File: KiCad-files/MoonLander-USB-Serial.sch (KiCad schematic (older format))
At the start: 7 parts, among them IC3 PRTR5V0U2X, IC4 CP2110-GM

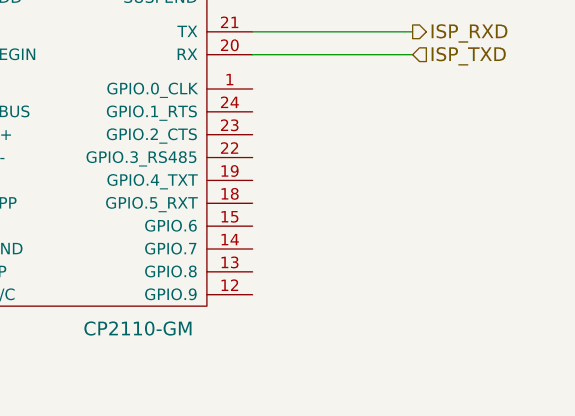
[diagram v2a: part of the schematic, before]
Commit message: drive ISP_ENTRY and RST from CP2110 GPIO outputs
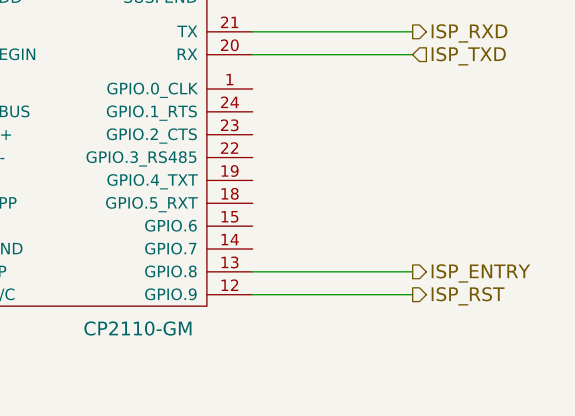
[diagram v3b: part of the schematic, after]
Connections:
- net ISP_RST: now reaches IC4.12 (GPIO.9)
- net ISP_ENTRY: now reaches IC4.13 (GPIO.8)
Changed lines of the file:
@@
 $EndComp
 $Comp
-L 5V_USB #PWR6
+L 5V_USB #PWR5
 U 1 1 565F94A8
 P 3100 3050
-F 0 "#PWR6" H 3100 2900 50  0001 C CNN
+F 0 "#PWR5" H 3100 2900 50  0001 C CNN
 F 1 "5V_USB" H 3100 3190 50  0000 C CNN
 F 2 "" H 3100 3050 60  0000 C CNN
@@
 $EndComp
 $Comp
-L GND #PWR7
+L GND #PWR6
 U 1 1 565F94C0
 P 3100 3400
-F 0 "#PWR7" H 3100 3150 50  0001 C CNN
+F 0 "#PWR6" H 3100 3150 50  0001 C CNN
 F 1 "GND" H 3100 3250 50  0000 C CNN
 F 2 "" H 3100 3400 50  0000 C CNN
@@
 	4650 4100 6200 4100
 $Comp
-L 5V_USB #PWR16
+L 5V_USB #PWR15
 U 1 1 565FB66D
 P 5000 3550
-F 0 "#PWR16" H 5000 3400 50  0001 C CNN
+F 0 "#PWR15" H 5000 3400 50  0001 C CNN
 F 1 "5V_USB" H 5000 3690 50  0000 C CNN
 F 2 "" H 5000 3550 60  0000 C CNN
@@
 	6050 3400 6200 3400
 $Comp
-L GND #PWR17
+L GND #PWR16
 U 1 1 565FBA98
 P 5000 4950
-F 0 "#PWR17" H 5000 4700 50  0001 C CNN
+F 0 "#PWR16" H 5000 4700 50  0001 C CNN
 F 1 "GND" H 5000 4800 50  0000 C CNN
 F 2 "" H 5000 4950 50  0000 C CNN
@@
 $EndComp
 $Comp
-L GND #PWR20
+L GND #PWR19
 U 1 1 565FBABC
 P 5400 3450
-F 0 "#PWR20" H 5400 3200 50  0001 C CNN
+F 0 "#PWR19" H 5400 3200 50  0001 C CNN
 F 1 "GND" H 5400 3300 50  0000 C CNN
 F 2 "" H 5400 3450 50  0000 C CNN
@@
 	5950 3150 5950 2900
 $Comp
-L VCC #PWR19
+L VCC #PWR18
 U 1 1 565FBB9F
 P 5400 2800
-F 0 "#PWR19" H 5400 2650 50  0001 C CNN
+F 0 "#PWR18" H 5400 2650 50  0001 C CNN
 F 1 "VCC" H 5400 2950 50  0000 C CNN
 F 2 "" H 5400 2800 50  0000 C CNN
@@
 	7800 3150 7800 3050
 $Comp
-L VCC #PWR26
+L VCC #PWR25
 U 1 1 565FC608
 P 7800 2650
-F 0 "#PWR26" H 7800 2500 50  0001 C CNN
+F 0 "#PWR25" H 7800 2500 50  0001 C CNN
 F 1 "VCC" H 7800 2800 50  0000 C CNN
 F 2 "" H 7800 2650 50  0000 C CNN
@@
 03 43 83 61 8C 09 03 03 03 03 43 83 61 8C 09 03 03 03 03 43 83 61 8C 09 03 03 03 03 43 83 61 03
 60 D2 64 32 30 30 30 30 34 84 CF 1C 00 A9 00 9C 01 A8 8B 59 19 06 06 06 06 06 E9 E3 33 80 C5 FF
-07 47 25 A5 D2 E9 03 52 D8 00 00 00 00 49 45 4E 44 AE 42 60 82 00
+07 47 25 A5 D2 E9 03 52 D8 00 00 00 00 49 45 4E 44 AE 42 60 82 7F
 EndData
 $EndBitmap
+Text HLabel 8300 4600 2    60   Output ~ 0
+ISP_ENTRY
+Wire Wire Line
+	8300 4600 7600 4600
+Wire Wire Line
+	7600 4700 8300 4700
+Text HLabel 8300 4700 2    60   Output ~ 0
+ISP_RST
 $EndSCHEMATC
